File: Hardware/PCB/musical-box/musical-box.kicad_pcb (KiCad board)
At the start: 4 copper layers, 70 x 60 mm, 184 parts, among them J1 power, J201 PSU, J202 Jack-DC, J203 Li Ion 2S, J401 SPI Display, J402 Rotary Encoder 1, J403 I2C Display, J404 Rotary Encoder 2, J405 WS2812, J501 spk_out, J502 aux in, J503 line in, P201 USB_C, P202 ICT-Point, P203 ICT-Point, P204 ICT-Point, Q201 DMP3017SFK, Q204 IRF9362, Q301 BC846BDW1, SW301 boot, SW302 reset, U201 STUSB4500QTR, U202 MP2615, U203 TPS56339, U204 TLV75733PDBV, U205 TLV75733PDBV, U206 TLV803EC30DBZR, U301 CH340C, U302 ESP32-WROVER, U401 PCF8574ATS, U501 SPH0644HM4H-1, U502 SPH0644HM4H-1, U503 TAS5754MDCA

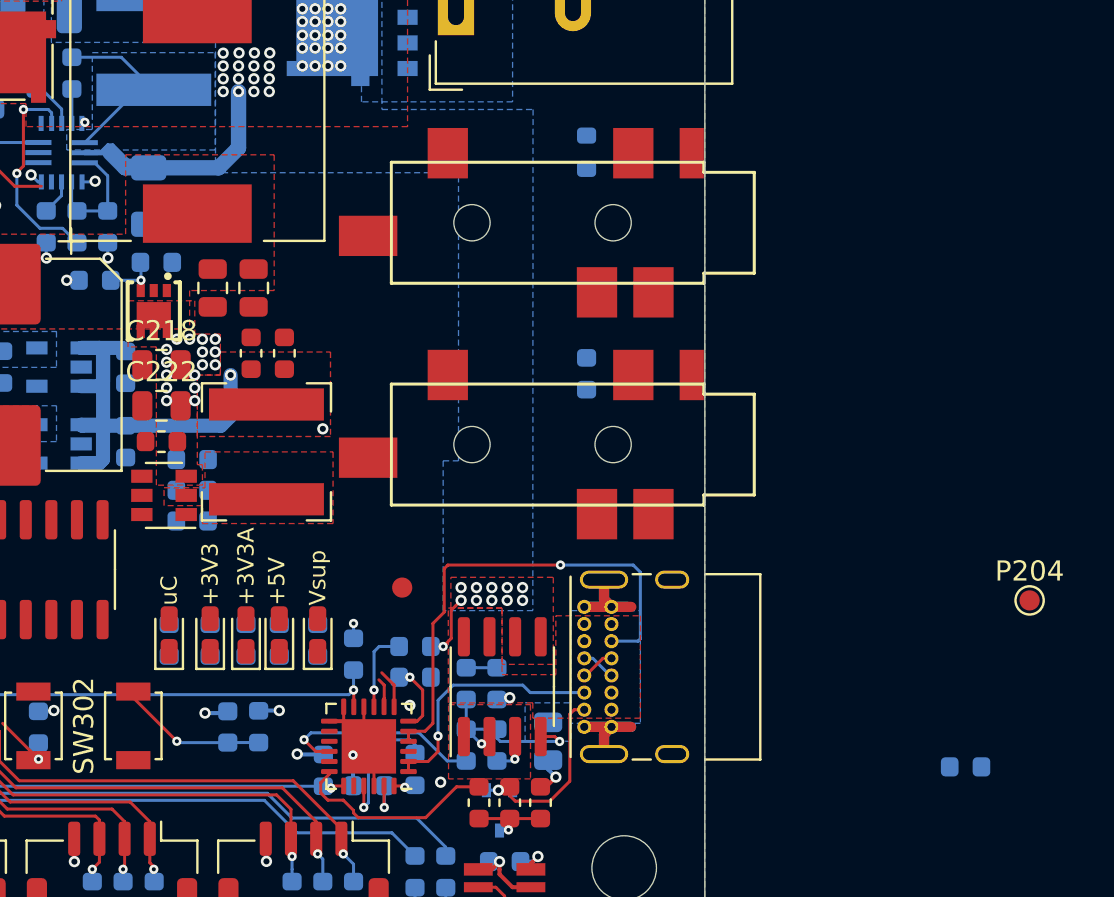
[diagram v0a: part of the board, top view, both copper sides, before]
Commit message: Route power LEDs
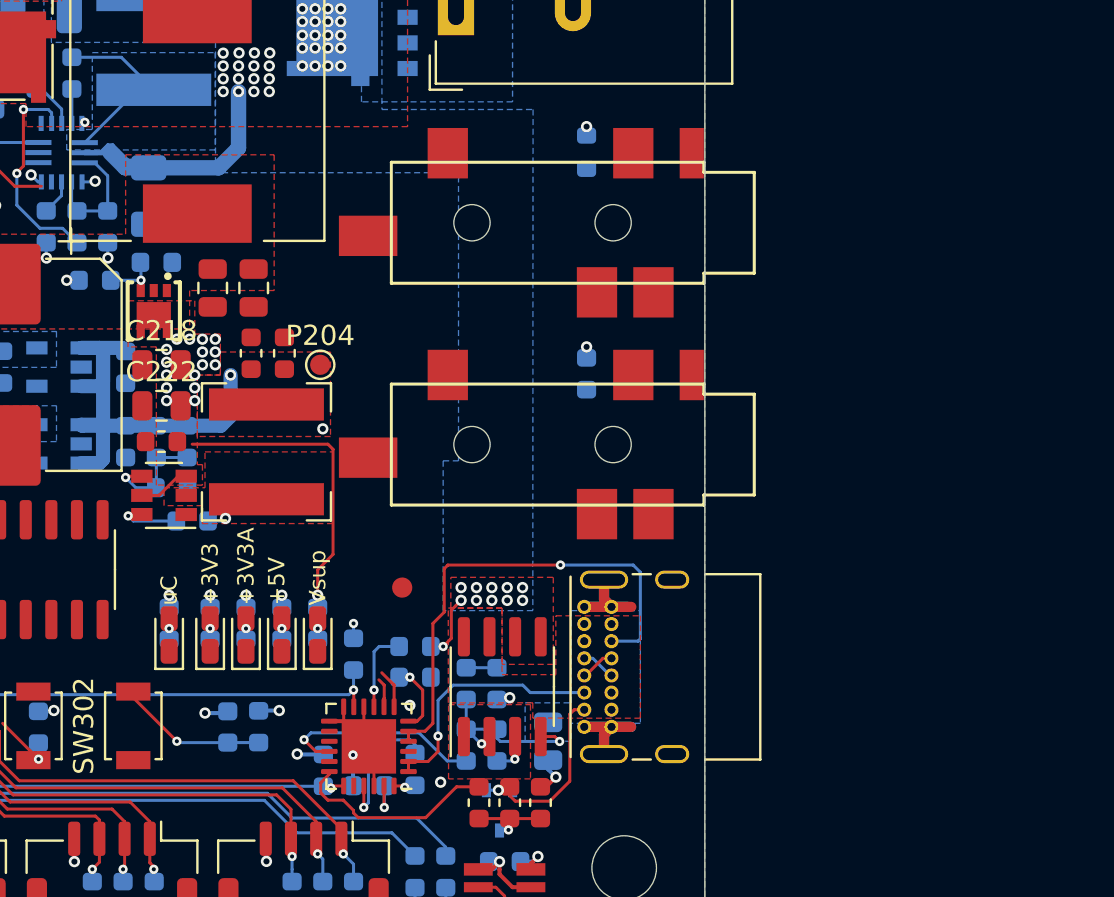
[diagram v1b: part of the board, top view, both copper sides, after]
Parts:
- moved R219 41.8 mm to (394.3, 159.9), turned to 270 degrees
- moved P204 37.1 mm to (400.9, 156.0)
- moved C219 1.99 mm to (392.8, 159.9), turned to 90 degrees
- moved R220 1.02 mm to (393.6, 162.1)
- moved R218 0.84 mm to (399.0, 168.9), turned to 90 degrees
- moved R105 0.83 mm to (393.4, 168.9), turned to 90 degrees
- moved R201 0.83 mm to (400.8, 168.9), turned to 90 degrees
- moved R217 0.83 mm to (395.5, 168.9), turned to 90 degrees
- moved R221 0.83 mm to (397.2, 168.9), turned to 90 degrees
- moved D208 0.13 mm to (399.0, 169.4)
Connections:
- R509 pad 2: +3.3VA -> +3V3
- R513 pad 2: +3.3VA -> +3V3
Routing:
- net +3.3VA: track 12.6 -> 52.7 mm, vias 9 -> 10
- net +15V: track 53.5 -> 71.3 mm, vias 30 -> 31
- net Net-(C219-Pad1): track 0.00 -> 5.57 mm, vias 0 -> 1
- net +5V: track 87.6 -> 93.1 mm, vias 14 -> 15
- net Net-(C216-Pad1): track 0.00 -> 3.20 mm, vias 0 -> 1
- net +3V3: track 34.5 -> 36.7 mm, vias 18 -> 22
- net Net-(D209-Pad2): track 0.00 -> 1.03 mm, vias 0 -> 1
- net Net-(D208-Pad2): track 0.00 -> 1.03 mm, vias 0 -> 1
- net Net-(D207-Pad2): track 0.00 -> 1.03 mm, vias 0 -> 1
- net Net-(D203-Pad2): track 0.00 -> 1.03 mm, vias 0 -> 1
- net Net-(D102-Pad2): track 0.00 -> 1.03 mm, vias 0 -> 1
- net Net-(C216-Pad2): track 0.00 -> 0.92 mm, vias 0 -> 1

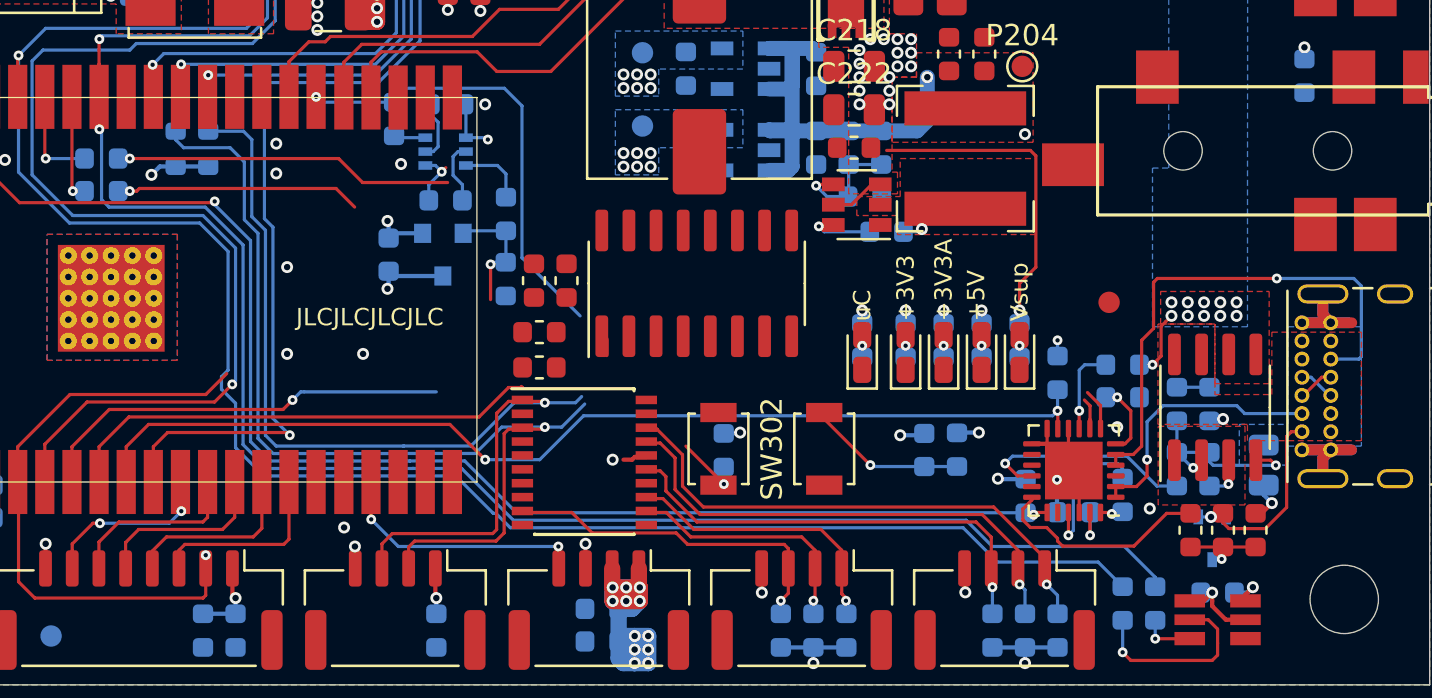
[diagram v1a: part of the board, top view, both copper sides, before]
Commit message: Route the USB-Serial converter and port expander
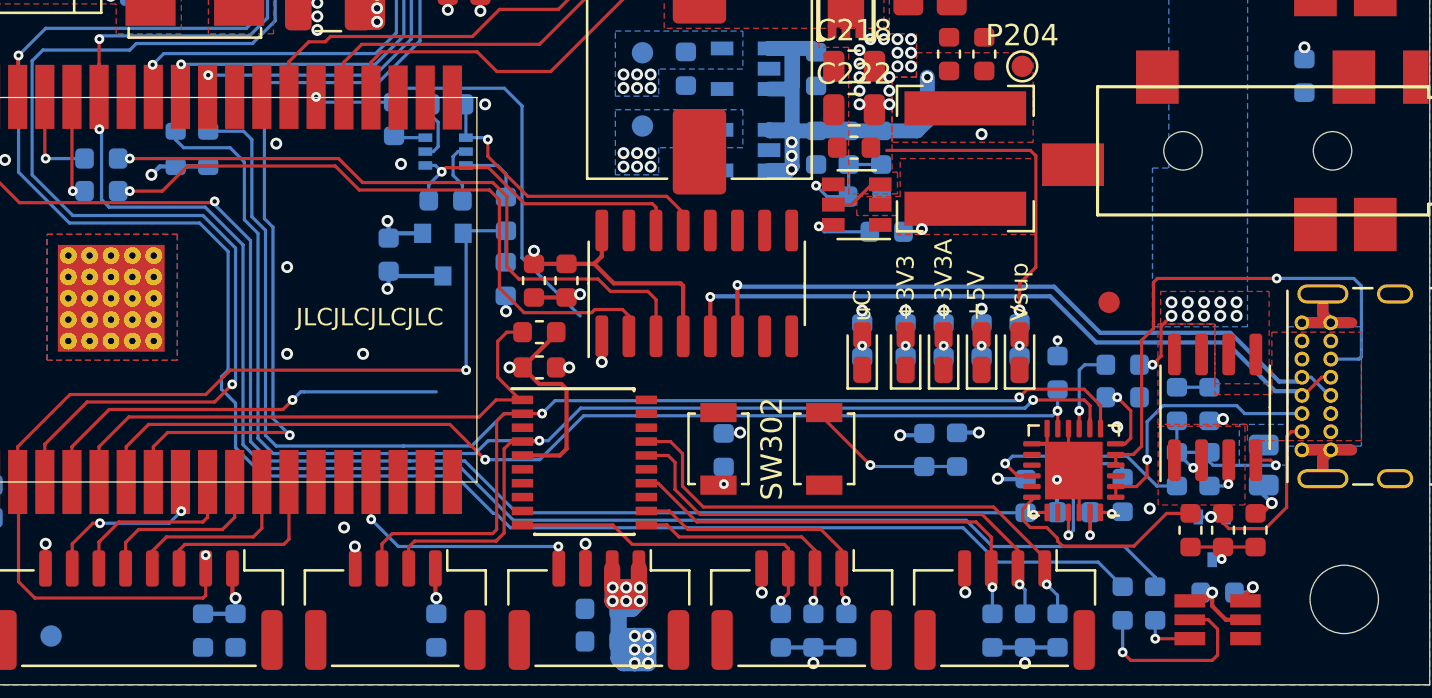
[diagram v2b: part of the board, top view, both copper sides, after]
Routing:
- net /Microcontroller/D+: track 1.70 -> 33.2 mm, vias 0 -> 1
- net /Microcontroller/D-: track 1.70 -> 32.5 mm, vias 0 -> 1
- net /Microcontroller/IO05: track 74.9 -> 98.1 mm, vias 3 -> 4
- net +3V3: track 36.7 -> 59.9 mm, vias 22 -> 25
- net /Microcontroller/IO18: track 75.1 -> 97.6 mm, vias 3 -> 4
- net Net-(R302-Pad2): track 11.5 -> 30.8 mm
- net Net-(R303-Pad2): track 15.9 -> 31.6 mm
- net +3.3VA: track 52.7 -> 37.6 mm
- net /Microcontroller/~RESET: track 37.9 -> 51.1 mm
- net /Microcontroller/DTR: track 2.73 -> 14.6 mm
- net /Microcontroller/RTS: track 2.75 -> 14.4 mm
- net +5V: track 93.1 -> 85.4 mm, vias 15 -> 18
- net /Microcontroller/I34: track 22.7 -> 27.0 mm
- net GND: track 119.0 -> 122.3 mm, vias 60 -> 61
- net Net-(J404-Pad2): track 24.6 -> 23.1 mm
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
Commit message: Route the VDD3A lines
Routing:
- net +3.3VA: track 37.6 -> 106.8 mm
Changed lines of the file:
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@@
     (thickness 1.6)
     (drawings 12)
-    (tracks 1554)
+    (tracks 1570)
     (zones 0)
     (modules 184)
@@
   (layers
     (0 F.Cu signal)
-    (1 In1.Cu signal hide)
-    (2 In2.Cu signal)
+    (1 In1.Cu signal)
+    (2 In2.Cu signal hide)
     (31 B.Cu signal)
     (34 B.Paste user hide)
@@
   (segment (start 397.244 168.0835) (end 397.244 167.474) (width 0.15) (layer B.Cu) (net 4))
   (segment (start 396.863 159.219) (end 397.244 159.6) (width 0.15) (layer In1.Cu) (net 4))
-  (segment (start 393.307 159.219) (end 396.863 159.219) (width 0.15) (layer In1.Cu) (net 4))
-  (segment (start 391.91 157.822) (end 393.307 159.219) (width 0.15) (layer In1.Cu) (net 4))
-  (segment (start 383.782 157.822) (end 391.91 157.822) (width 0.15) (layer In1.Cu) (net 4))
-  (segment (start 383.528 158.076) (end 383.782 157.822) (width 0.15) (layer In1.Cu) (net 4))
-  (segment (start 383.528 160.108) (end 383.528 158.076) (width 0.15) (layer In1.Cu) (net 4))
   (segment (start 397.244 167.474) (end 397.244 159.6) (width 0.15) (layer In1.Cu) (net 4))
+  (segment (start 378.829 147.408) (end 378.829 149.313) (width 0.2) (layer In1.Cu) (net 4))
+  (segment (start 379.21 149.694) (end 396.736 149.694) (width 0.2) (layer In1.Cu) (net 4))
+  (segment (start 378.829 149.313) (end 379.21 149.694) (width 0.2) (layer In1.Cu) (net 4))
+  (segment (start 396.736 149.694) (end 397.117 150.075) (width 0.2) (layer In1.Cu) (net 4))
+  (segment (start 397.117 158.965) (end 396.863 159.219) (width 0.2) (layer In1.Cu) (net 4))
+  (segment (start 397.117 150.075) (end 397.117 158.965) (width 0.2) (layer In1.Cu) (net 4))
+  (segment (start 396.863 159.219) (end 393.18 159.219) (width 0.2) (layer In1.Cu) (net 4))
+  (segment (start 393.18 159.219) (end 391.656 157.695) (width 0.2) (layer In1.Cu) (net 4))
+  (segment (start 391.656 157.695) (end 384.036 157.695) (width 0.2) (layer In1.Cu) (net 4))
+  (segment (start 383.528 158.203) (end 383.528 160.108) (width 0.2) (layer In1.Cu) (net 4))
+  (segment (start 384.036 157.695) (end 383.528 158.203) (width 0.2) (layer In1.Cu) (net 4))
+  (segment (start 378.829 131.8235) (end 378.829 147.408) (width 0.2) (layer In1.Cu) (net 4))
+  (segment (start 378.309 131.3035) (end 378.829 131.8235) (width 0.2) (layer In1.Cu) (net 4))
+  (segment (start 398.006 168.236) (end 397.244 167.474) (width 0.2) (layer In1.Cu) (net 4))
+  (segment (start 406.261 171.03) (end 403.467 168.236) (width 0.2) (layer In1.Cu) (net 4))
+  (segment (start 407.531 171.03) (end 406.261 171.03) (width 0.2) (layer In1.Cu) (net 4))
+  (segment (start 407.912 171.411) (end 407.531 171.03) (width 0.2) (layer In1.Cu) (net 4))
+  (segment (start 407.912 179.92) (end 407.912 171.411) (width 0.2) (layer In1.Cu) (net 4))
+  (segment (start 408.674 180.682) (end 407.912 179.92) (width 0.2) (layer In1.Cu) (net 4))
+  (segment (start 403.467 168.236) (end 398.006 168.236) (width 0.2) (layer In1.Cu) (net 4))
+  (segment (start 409.817 180.682) (end 408.674 180.682) (width 0.2) (layer In1.Cu) (net 4))
   (segment (start 396.341 174.779) (end 396.34 174.78) (width 0.15) (layer B.Cu) (net 5))
   (segment (start 397.872 174.779) (end 396.341 174.779) (width 0.15) (layer B.Cu) (net 5))

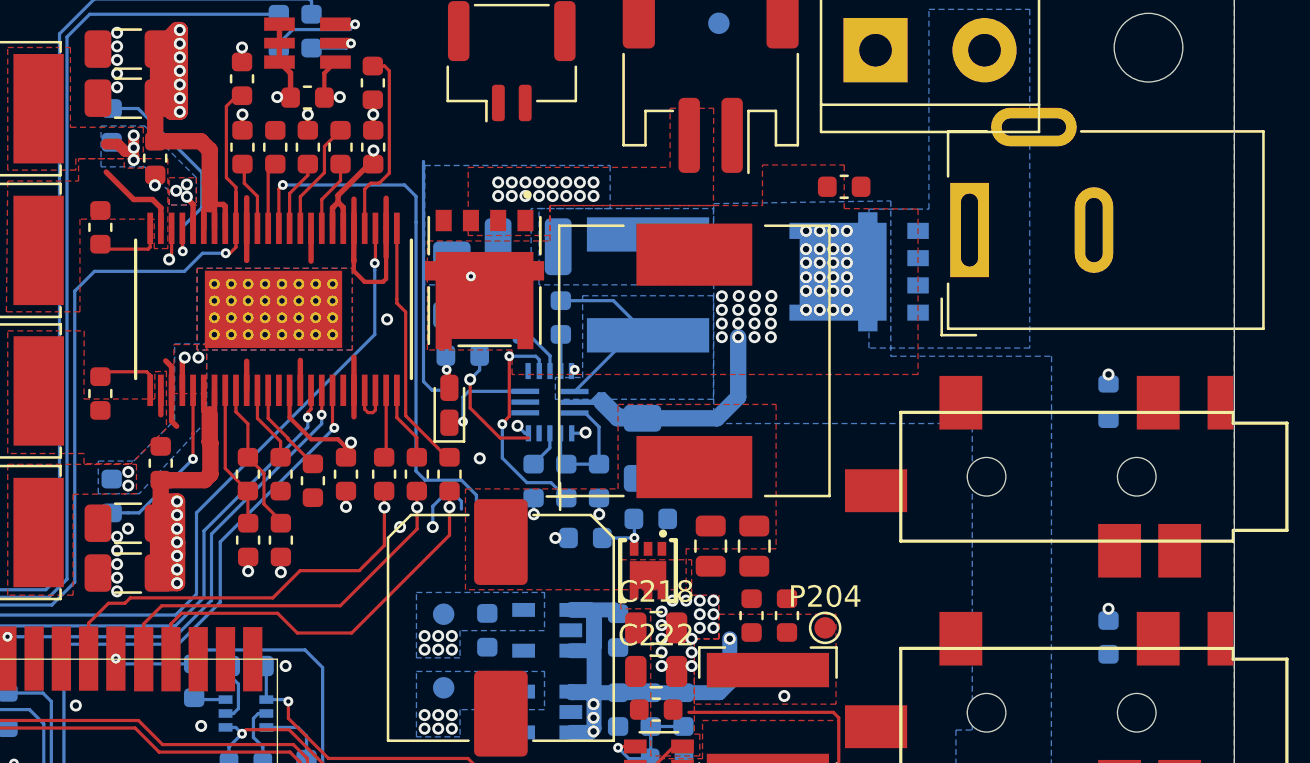
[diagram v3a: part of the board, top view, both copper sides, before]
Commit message: Route audio signals
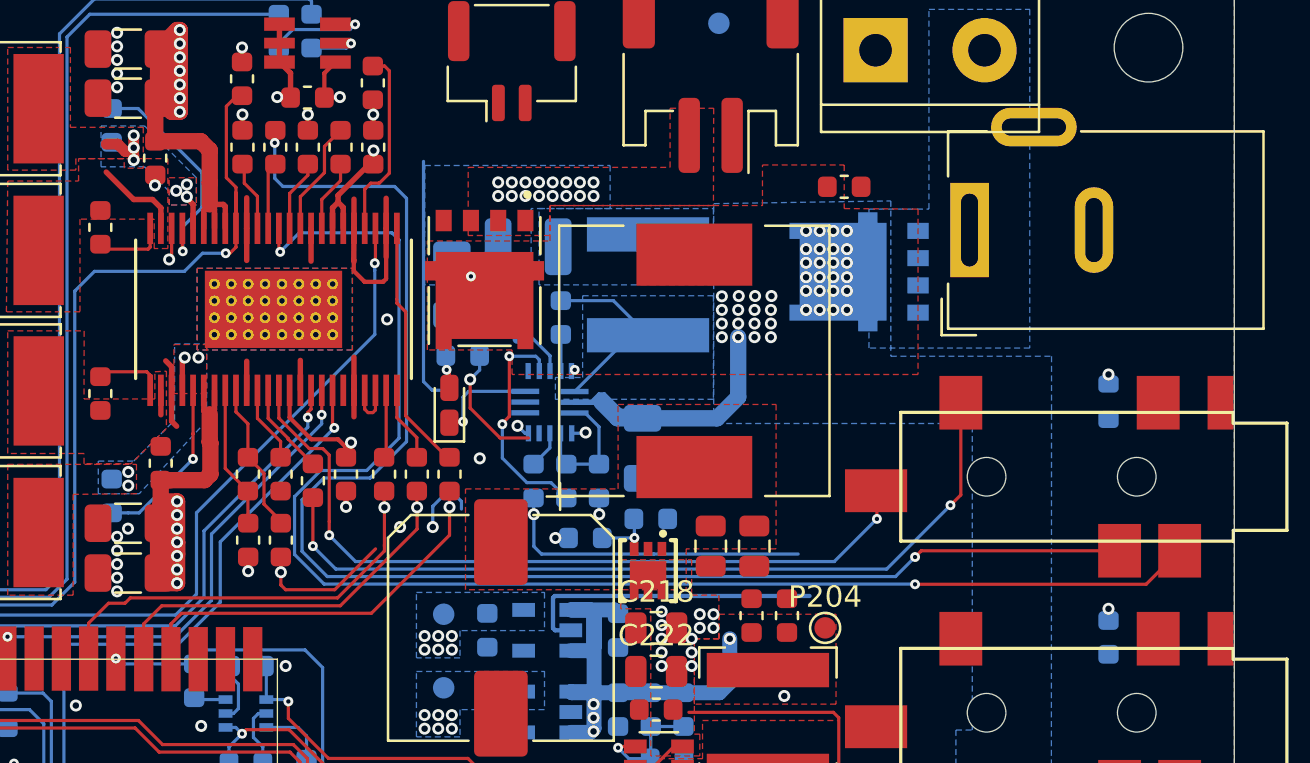
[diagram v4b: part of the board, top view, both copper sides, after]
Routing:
- net /Audio Output/SPK_INB: track 0.00 -> 67.6 mm, vias 0 -> 2
- net /Audio Output/DAC_OUTB: track 28.3 -> 67.6 mm, vias 1 -> 2
- net /Audio Output/SPK_INA: track 0.00 -> 38.6 mm, vias 0 -> 2
- net /Audio Output/DAC_OUTA: track 0.00 -> 36.3 mm, vias 0 -> 2
- net GND: track 122.3 -> 156.5 mm
- net /Microcontroller/IO15: track 19.2 -> 18.4 mm
- net +15V: vias 31 -> 27
